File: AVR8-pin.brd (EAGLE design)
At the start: 16.5 x 17.1 mm, 4 parts

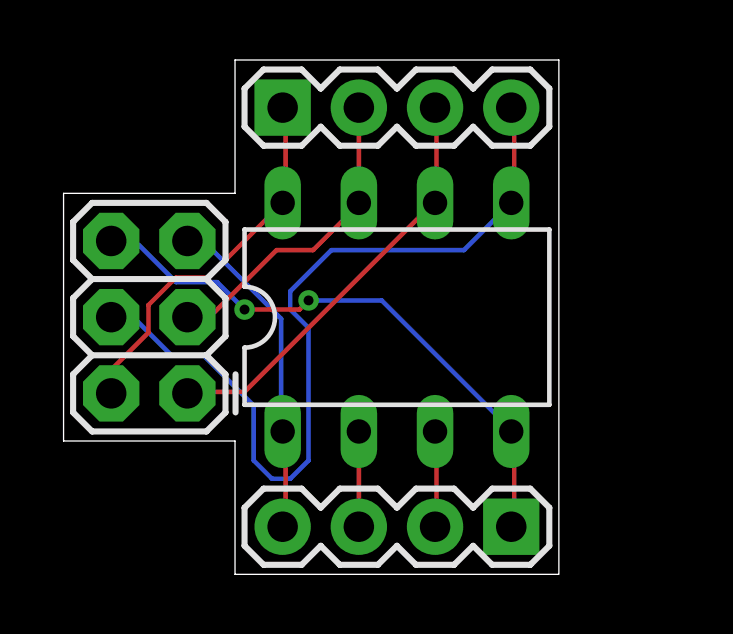
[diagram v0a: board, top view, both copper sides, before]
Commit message: Oriented the AVR header correctly instead of the jacked up usbtinyisp cable
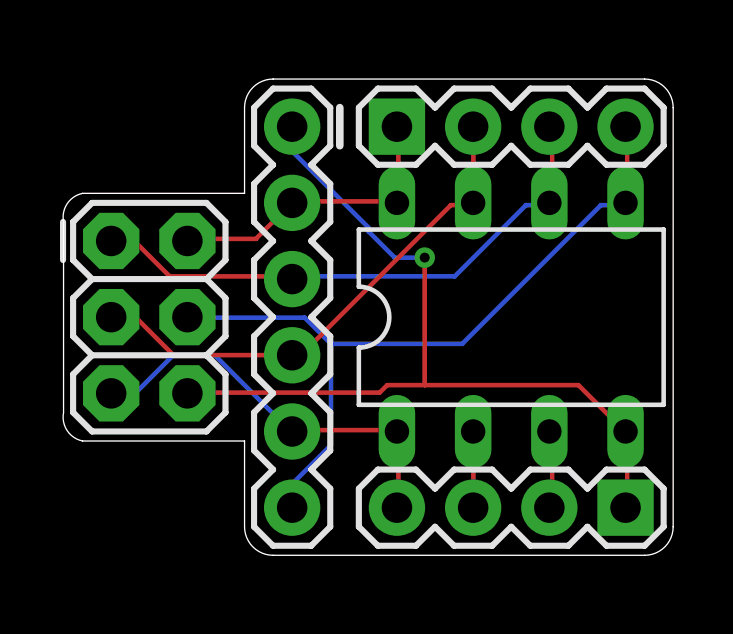
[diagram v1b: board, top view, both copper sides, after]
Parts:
- added JP1: (no value), SparkFun-Connectors:1X06
- moved AVR 5.68 mm to (3.17, 11.4), turned to 270 degrees
- moved LEFT 3.86 mm to (20.3, 2.54)
- moved RIGHT 3.86 mm to (12.7, 15.2)
- moved IC1 3.81 mm to (16.5, 8.89)
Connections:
- net GND: now also JP1.6
- net PIN1: now also JP1.2
- net PIN5: now also JP1.1
- net PIN6: now also JP1.4
- net PIN7: now also JP1.3
- net VCC: now also JP1.5
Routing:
- net GND: track 19.5 -> 28.9 mm, vias 2 -> 1
- net PIN7: track 10.5 -> 17.2 mm
- net PIN6: track 14.1 -> 18.9 mm
- net VCC: track 12.6 -> 10.1 mm
- net PIN1: track 11.3 -> 13.7 mm
- net PIN5: track 27.9 -> 25.5 mm
- net PIN2: track 3.17 -> 2.54 mm
- net PIN3: track 3.21 -> 2.63 mm
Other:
- board size 16.5 x 17.1 mm -> 20.3 x 15.9 mm
- board text added: "v2"

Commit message: Adjusted for a fix that was not a fix
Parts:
- moved AVR 5.68 mm to (5.71, 6.35), turned to 90 degrees
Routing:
- net VCC: track 10.1 -> 15.9 mm
- net PIN5: track 25.5 -> 27.7 mm, vias 0 -> 1
- net PIN7: track 17.2 -> 15.2 mm
- net PIN6: track 18.9 -> 17.5 mm, vias 0 -> 1
- net PIN1: track 13.7 -> 14.4 mm
- net GND: track 28.9 -> 28.3 mm, vias 1 -> 2
